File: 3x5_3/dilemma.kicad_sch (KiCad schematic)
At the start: 82 parts, among them J5001 BATTERY_CONN_DEANS, J5011 BATTERY_CONN_DEANS, SW101 NA_SW_Push, SW102 NA_SW_Push, SW103 NA_SW_Push, SW104 NA_SW_Push, SW105 NA_SW_Push, SW106 NA_SW_Push, SW107 NA_SW_Push, SW108 NA_SW_Push, SW109 NA_SW_Push, SW112 NA_SW_Push, SW113 NA_SW_Push, SW114 NA_SW_Push, SW115 NA_SW_Push, SW116 NA_SW_Push, SW117 NA_SW_Push, SW118 NA_SW_Push, SW119 NA_SW_Push, SW3001 NA_SW_Push, SW5002 NA_SW_Push, SW5003 NA_SW_Push, SW5004 NA_SW_Push, SW5005 NA_SW_Push, SW5006 NA_SW_Push, SW5007 NA_SW_Push, SW5008 NA_SW_Push, SW5009 NA_SW_Push, SW5010 NA_SW_Push, SW5011 NA_SW_Push, SW5012 NA_SW_Push, SW5013 NA_SW_Push, SW5014 NA_SW_Push, SW5015 NA_SW_Push, SW5016 NA_SW_Push, SW5017 NA_SW_Push, SW5018 NA_SW_Push, SW5019 NA_SW_Push, SW5021 SW_SPST, SW5022 SW_SPST, U5001 eliteC, U5007 eliteC

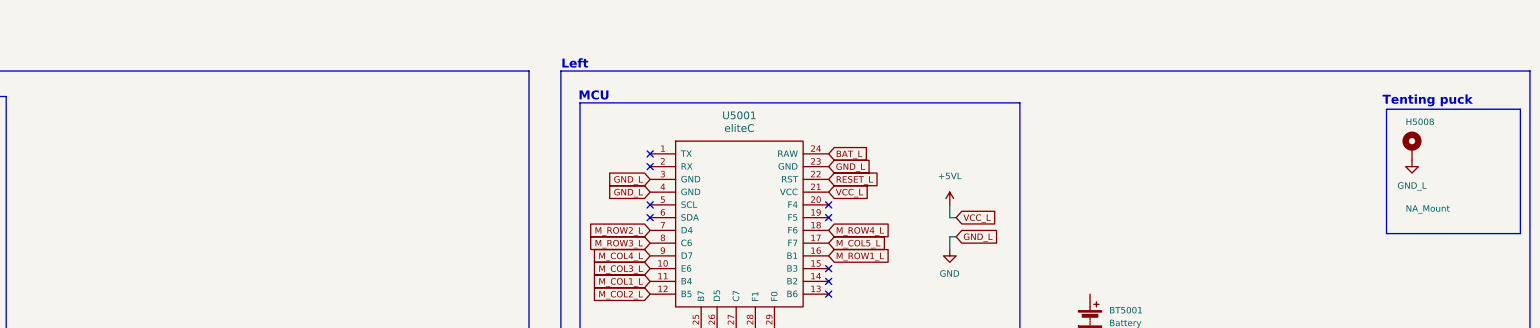
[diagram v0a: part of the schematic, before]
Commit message: add right mounting holes
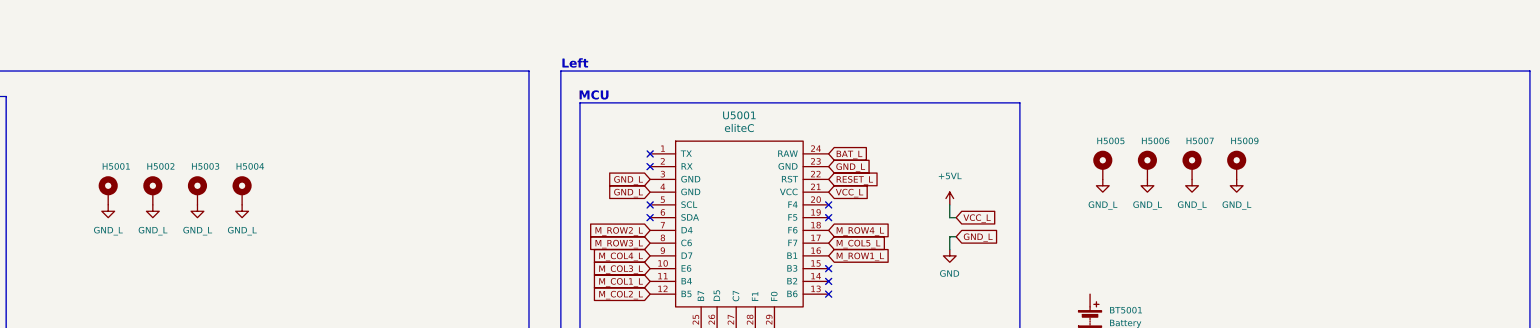
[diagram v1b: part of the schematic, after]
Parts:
- removed H5008: NA_Mount, local-libraries:Tenting_Puck, symbol Mechanical:MountingHole_Pad
- added H5001, H5002, H5003, H5004, H5005, H5006, H5007, H5009: NA_Mount, local-libraries:M2_Mounting_Hole, symbol Mechanical:MountingHole_Pad
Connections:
- net GND: now also H5001.1, H5002.1, H5003.1, H5004.1, H5005.1, H5006.1, H5007.1, H5009.1
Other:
- note removed: "Tenting puck"
